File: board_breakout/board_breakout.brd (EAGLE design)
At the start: 160 x 100 mm, 3 parts

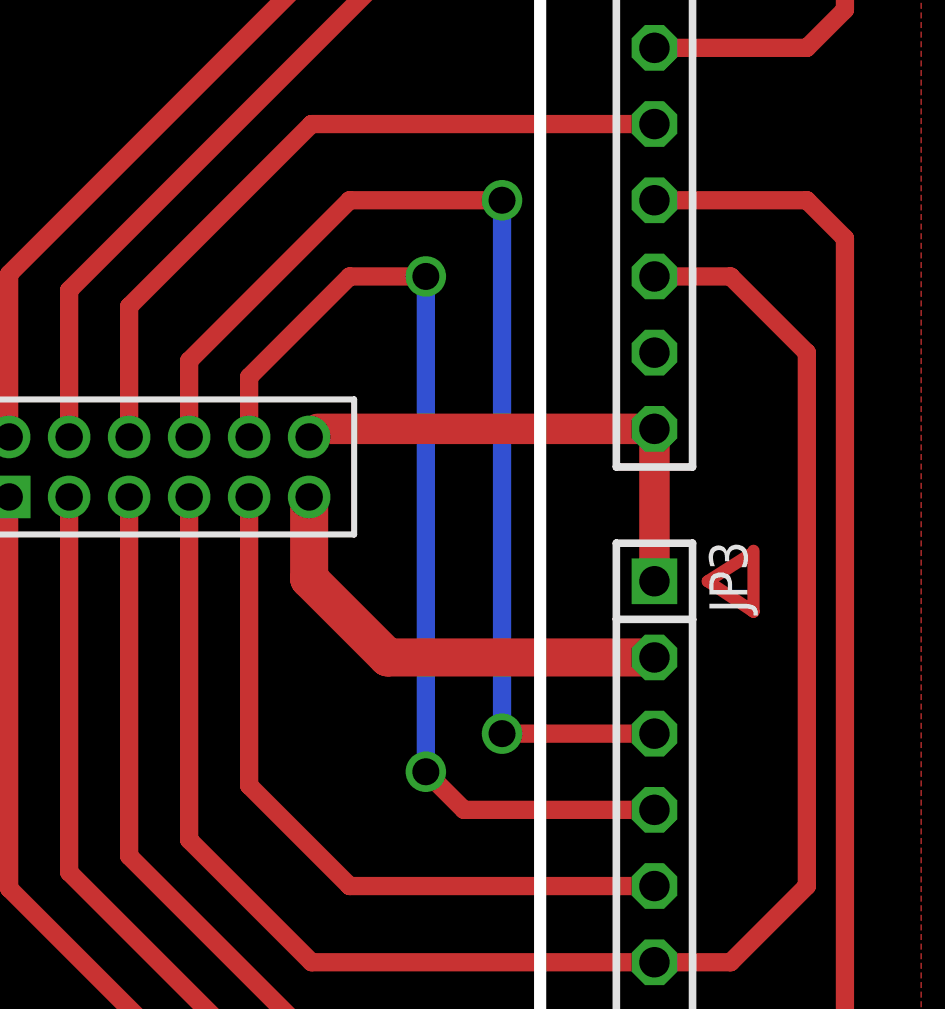
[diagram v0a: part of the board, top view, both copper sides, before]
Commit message: breakout board now one-sided
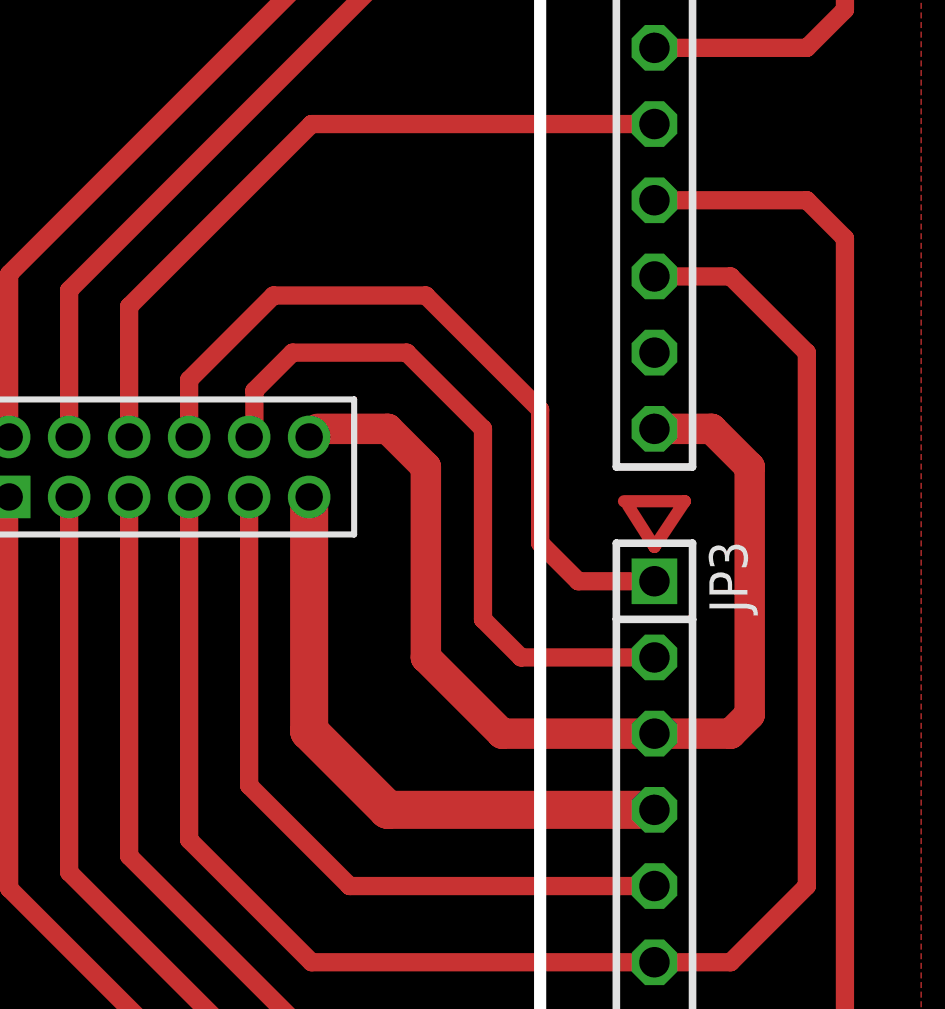
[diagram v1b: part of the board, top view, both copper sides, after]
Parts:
- JP2: value JTAG -> JTAG_Bottom
- JP3: value (none) -> Periph_Bottom
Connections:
- net 3V3: now also JP3.4; no longer JP3.2
- net GND: now also JP3.3; no longer JP3.1
- net SCL-EXT: now also JP3.2; no longer JP3.4
- net TX: now also JP3.1; no longer JP3.3
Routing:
- net GND: track 16.7 -> 34.9 mm
- net TX: track 38.0 -> 25.1 mm, vias 2 -> 0
- net SCL-EXT: track 33.9 -> 23.4 mm, vias 2 -> 0
- net 3V3: track 15.3 -> 20.4 mm
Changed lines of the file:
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@@
 <setting verticaltext="up"/>
 </settings>
-<grid distance="50" unitdist="mil" unit="mil" style="lines" multiple="1" display="no" altdistance="0.025" altunitdist="inch" altunit="inch"/>
+<grid distance="25" unitdist="mil" unit="mil" style="lines" multiple="1" display="no" altdistance="0.025" altunitdist="inch" altunit="inch"/>
 <layers>
 <layer number="1" name="Top" color="4" fill="1" visible="yes" active="yes"/>
@@
 </class>
 </classes>
-<designrules name="default">
+<designrules name="default *">
 <description language="de">&lt;b&gt;EAGLE Design Rules&lt;/b&gt;
 &lt;p&gt;
@@
 <param name="mtCopper" value="0.035mm 0.035mm 0.035mm 0.035mm 0.035mm 0.035mm 0.035mm 0.035mm 0.035mm 0.035mm 0.035mm 0.035mm 0.035mm 0.035mm 0.035mm 0.035mm"/>
 <param name="mtIsolate" value="1.5mm 0.15mm 0.2mm 0.15mm 0.2mm 0.15mm 0.2mm 0.15mm 0.2mm 0.15mm 0.2mm 0.15mm 0.2mm 0.15mm 0.2mm"/>
-<param name="mdWireWire" value="8mil"/>
-<param name="mdWirePad" value="8mil"/>
-<param name="mdWireVia" value="8mil"/>
-<param name="mdPadPad" value="8mil"/>
-<param name="mdPadVia" value="8mil"/>
-<param name="mdViaVia" value="8mil"/>
-<param name="mdSmdPad" value="8mil"/>
-<param name="mdSmdVia" value="8mil"/>
-<param name="mdSmdSmd" value="8mil"/>
+<param name="mdWireWire" value="12mil"/>
+<param name="mdWirePad" value="12mil"/>
+<param name="mdWireVia" value="12mil"/>
+<param name="mdPadPad" value="12mil"/>
+<param name="mdPadVia" value="12mil"/>
+<param name="mdViaVia" value="12mil"/>
+<param name="mdSmdPad" value="12mil"/>
+<param name="mdSmdVia" value="12mil"/>
+<param name="mdSmdSmd" value="12mil"/>
 <param name="mdViaViaSameLayer" value="8mil"/>
 <param name="mnLayersViaInSmd" value="2"/>
 <param name="mdCopperDimension" value="40mil"/>
-<param name="mdDrill" value="8mil"/>
+<param name="mdDrill" value="12mil"/>
 <param name="mdSmdStop" value="0mil"/>
 <param name="msWidth" value="10mil"/>
@@
 <elements>
 <element name="JP1" library="pinhead" package="2X06M" value="SKYNET" x="40.64" y="46.99"/>
-<element name="JP2" library="pinhead" package="1X08" value="JTAG" x="57.15" y="57.15" rot="R270"/>
-<element name="JP3" library="pinhead" package="1X10" value="" x="57.15" y="31.75" rot="R270"/>
+<element name="JP2" library="pinhead" package="1X08" value="JTAG_Bottom" x="57.15" y="57.15" rot="R270"/>
+<element name="JP3" library="pinhead" package="1X10" value="Periph_Bottom" x="57.15" y="31.75" rot="R270"/>
 </elements>
 <signals>
 <signal name="3V3">
 <contactref element="JP1" pad="11"/>
-<contactref element="JP3" pad="2"/>
-<wire x1="45.64" y1="45.99" x2="45.64" y2="43.26" width="1.27" layer="1"/>
-<wire x1="45.64" y1="43.26" x2="48.26" y2="40.64" width="1.27" layer="1"/>
-<wire x1="48.26" y1="40.64" x2="57.15" y2="40.64" width="1.27" layer="1"/>
+<contactref element="JP3" pad="4"/>
+<wire x1="45.64" y1="45.99" x2="45.64" y2="38.18" width="1.27" layer="1"/>
+<wire x1="45.64" y1="38.18" x2="48.26" y2="35.56" width="1.27" layer="1"/>
+<wire x1="48.26" y1="35.56" x2="57.15" y2="35.56" width="1.27" layer="1"/>
 </signal>
 <signal name="GND">
 <contactref element="JP1" pad="12"/>
 <contactref element="JP2" pad="8"/>
-<wire x1="57.15" y1="48.26" x2="45.91" y2="48.26" width="1.016" layer="1"/>
 <wire x1="45.91" y1="48.26" x2="45.64" y2="47.99" width="0.6096" layer="1"/>
-<contactref element="JP3" pad="1"/>
-<wire x1="57.15" y1="48.26" x2="57.15" y2="43.18" width="1.016" layer="1"/>
 <polygon width="0.4064" layer="1" isolate="1.016" orphans="yes">
 <vertex x="33.02" y="71.12"/>
@@
 <vertex x="33.02" y="72.39"/>
 </polygon>
+<contactref element="JP3" pad="3"/>
+<wire x1="45.91" y1="48.26" x2="48.26" y2="48.26" width="1.016" layer="1"/>
+<wire x1="48.26" y1="48.26" x2="49.53" y2="46.99" width="1.016" layer="1"/>
+<wire x1="49.53" y1="46.99" x2="49.53" y2="40.64" width="1.016" layer="1"/>
+<wire x1="49.53" y1="40.64" x2="52.07" y2="38.1" width="1.016" layer="1"/>
+<wire x1="52.07" y1="38.1" x2="57.15" y2="38.1" width="1.016" layer="1"/>
+<wire x1="57.15" y1="48.26" x2="59.055" y2="48.26" width="1.016" layer="1"/>
+<wire x1="59.055" y1="48.26" x2="60.325" y2="46.99" width="1.016" layer="1"/>
+<wire x1="60.325" y1="46.99" x2="60.325" y2="38.735" width="1.016" layer="1"/>
+<wire x1="60.325" y1="38.735" x2="59.69" y2="38.1" width="1.016" layer="1"/>
+<wire x1="59.69" y1="38.1" x2="57.15" y2="38.1" width="1.016" layer="1"/>
 </signal>
 <signal name="TX">
 <contactref element="JP1" pad="8"/>
-<wire x1="41.64" y1="47.99" x2="41.64" y2="50.53" width="0.6096" layer="1"/>
-<wire x1="41.64" y1="50.53" x2="46.99" y2="55.88" width="0.6096" layer="1"/>
-<wire x1="46.99" y1="55.88" x2="52.07" y2="55.88" width="0.6096" layer="1"/>
-<via x="52.07" y="55.88" extent="1-16" drill="0.9"/>
-<contactref element="JP3" pad="3"/>
-<wire x1="57.15" y1="38.1" x2="52.07" y2="38.1" width="0.6096" layer="1"/>
-<via x="52.07" y="38.1" extent="1-16" drill="0.9"/>
-<wire x1="52.07" y1="38.1" x2="52.07" y2="55.88" width="0.6096" layer="16"/>
+<contactref element="JP3" pad="1"/>
+<wire x1="41.64" y1="47.99" x2="41.64" y2="49.895" width="0.6096" layer="1"/>
+<wire x1="41.64" y1="49.895" x2="44.45" y2="52.705" width="0.6096" layer="1"/>
+<wire x1="44.45" y1="52.705" x2="49.53" y2="52.705" width="0.6096" layer="1"/>
+<wire x1="49.53" y1="52.705" x2="53.34" y2="48.895" width="0.6096" layer="1"/>
+<wire x1="53.34" y1="48.895" x2="53.34" y2="44.45" width="0.6096" layer="1"/>
+<wire x1="53.34" y1="44.45" x2="54.61" y2="43.18" width="0.6096" layer="1"/>
+<wire x1="54.61" y1="43.18" x2="57.15" y2="43.18" width="0.6096" layer="1"/>
 </signal>
 <signal name="JTAG_TDO">
@@
 <signal name="SCL-EXT">
 <contactref element="JP1" pad="10"/>
-<wire x1="43.64" y1="47.99" x2="43.64" y2="49.99" width="0.6096" layer="1"/>
-<wire x1="43.64" y1="49.99" x2="46.99" y2="53.34" width="0.6096" layer="1"/>
-<wire x1="46.99" y1="53.34" x2="49.53" y2="53.34" width="0.6096" layer="1"/>
-<via x="49.53" y="53.34" extent="1-16" drill="0.9"/>
-<contactref element="JP3" pad="4"/>
-<wire x1="57.15" y1="35.56" x2="50.8" y2="35.56" width="0.6096" layer="1"/>
-<wire x1="50.8" y1="35.56" x2="49.53" y2="36.83" width="0.6096" layer="1"/>
-<via x="49.53" y="36.83" extent="1-16" drill="0.9"/>
-<wire x1="49.53" y1="36.83" x2="49.53" y2="53.34" width="0.6096" layer="16"/>
+<contactref element="JP3" pad="2"/>
+<wire x1="57.15" y1="40.64" x2="52.705" y2="40.64" width="0.6096" layer="1"/>
+<wire x1="52.705" y1="40.64" x2="51.435" y2="41.91" width="0.6096" layer="1"/>
+<wire x1="51.435" y1="41.91" x2="51.435" y2="48.26" width="0.6096" layer="1"/>
+<wire x1="51.435" y1="48.26" x2="48.895" y2="50.8" width="0.6096" layer="1"/>
+<wire x1="48.895" y1="50.8" x2="45.085" y2="50.8" width="0.6096" layer="1"/>
+<wire x1="45.085" y1="50.8" x2="43.815" y2="49.53" width="0.6096" layer="1"/>
+<wire x1="43.815" y1="49.53" x2="43.815" y2="48.165" width="0.6096" layer="1"/>
+<wire x1="43.815" y1="48.165" x2="43.64" y2="47.99" width="0.6096" layer="1"/>
 </signal>
 <signal name="N$8">
@@
 </signal>
 <signal name="N$2">
-<wire x1="60.452" y1="44.196" x2="60.452" y2="42.164" width="0.4064" layer="1"/>
-<wire x1="60.452" y1="42.164" x2="58.928" y2="43.18" width="0.4064" layer="1"/>
-<wire x1="58.928" y1="43.18" x2="60.325" y2="44.069" width="0.4064" layer="1"/>
+<wire x1="56.134" y1="45.847" x2="58.166" y2="45.847" width="0.4064" layer="1"/>
+<wire x1="58.166" y1="45.847" x2="57.15" y2="44.323" width="0.4064" layer="1"/>
+<wire x1="57.15" y1="44.323" x2="56.261" y2="45.72" width="0.4064" layer="1"/>
 </signal>
 </signals>

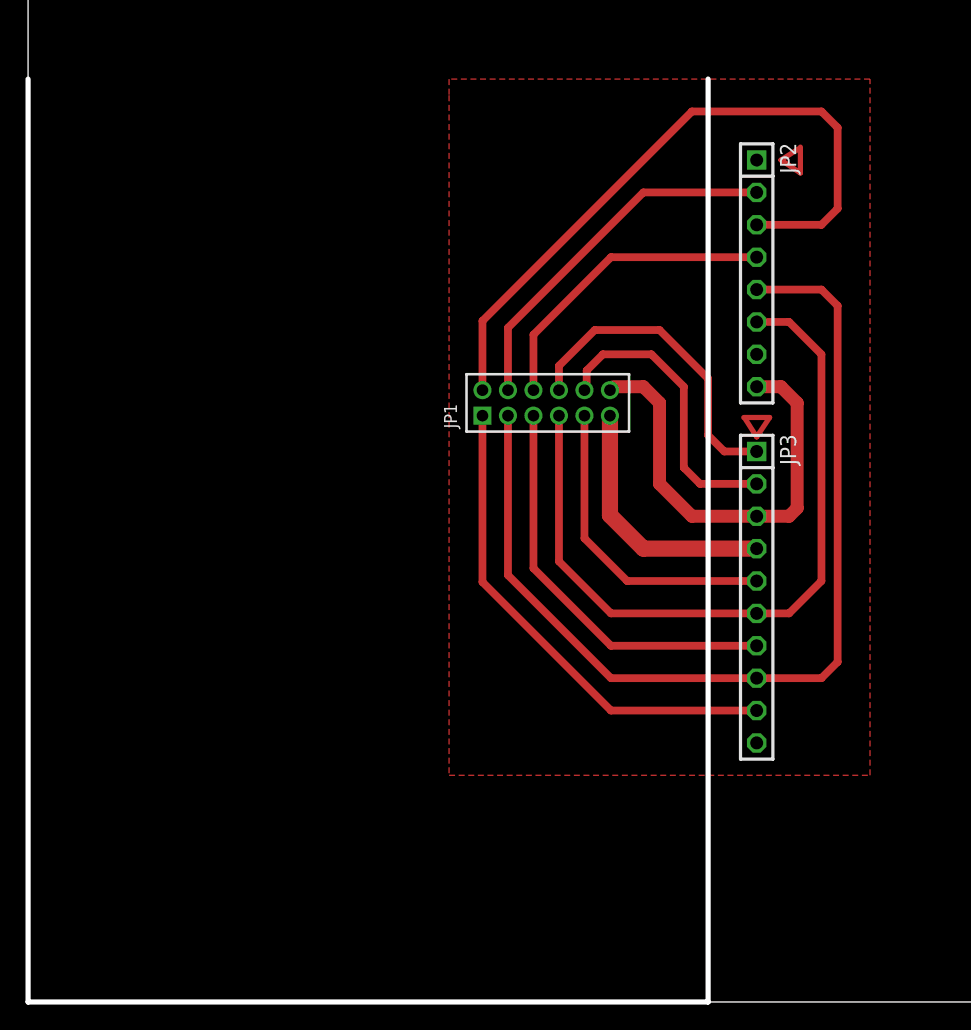
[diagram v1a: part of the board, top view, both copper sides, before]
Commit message: breakout board added header
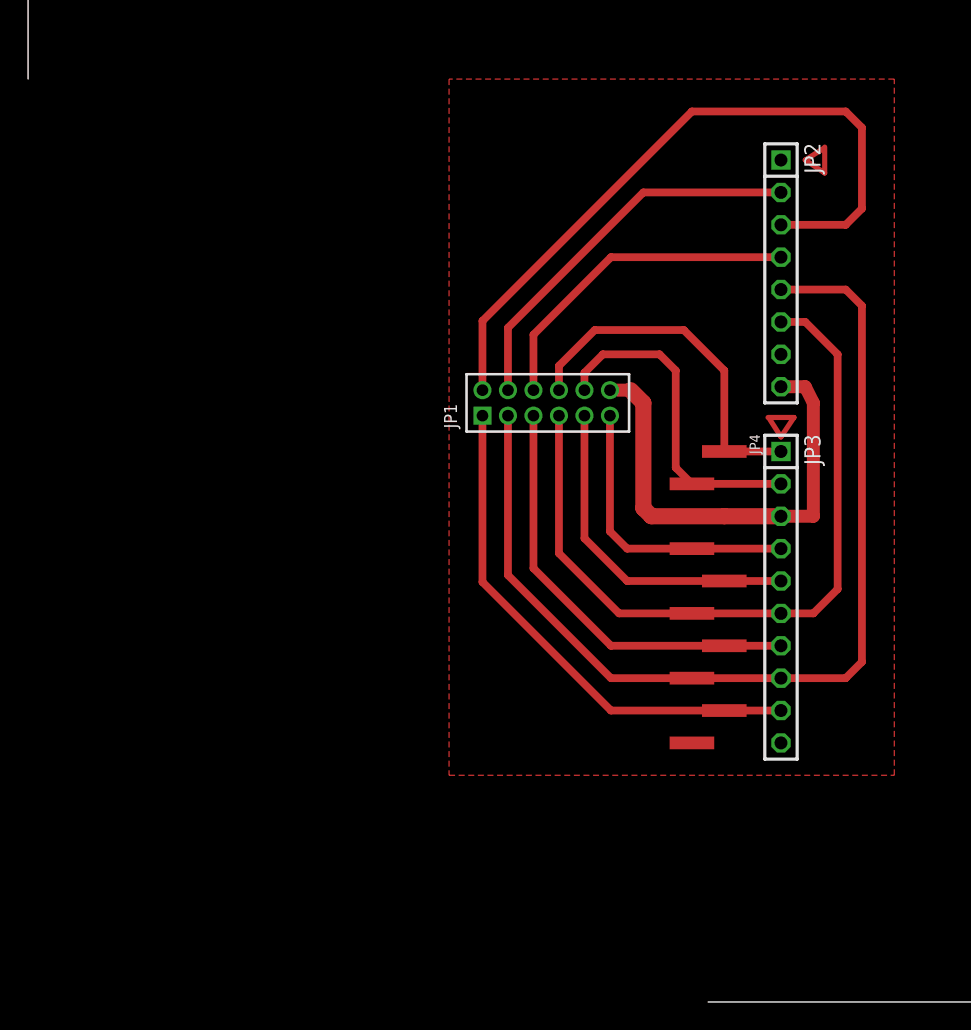
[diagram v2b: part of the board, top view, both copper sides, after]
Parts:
- added JP4: Periph_Top, microbuilder:1X10_SMT
- moved JP2 1.91 mm to (59.1, 57.1)
- moved JP3 1.91 mm to (59.1, 31.8)
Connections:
- removed net N$10: JP3.8
- removed net N$8: JP3.6
- net 3V3: now also JP4.4
- net AD-EXT: now also JP4.9
- net GND: now also JP4.3
- net JTAG_TDI: now also JP3.8, JP4.8
- net RESET: now also JP3.6, JP4.6
- net RX: now also JP4.7
- net SCL-EXT: now also JP4.2
- net SDA-EXT: now also JP4.5
- net TX: now also JP4.1
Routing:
- net TX: track 25.1 -> 28.1 mm
- net 3V3: track 20.4 -> 23.1 mm
- net SCL-EXT: track 23.4 -> 26.1 mm
- net GND: track 34.9 -> 37.1 mm
- net SDA-EXT: track 24.5 -> 26.4 mm
- net RX: track 32.0 -> 33.9 mm
- net JTAG_TMS: track 28.8 -> 30.7 mm
- net JTAG_TDO: track 24.4 -> 26.3 mm
- net AD-EXT: track 38.7 -> 40.6 mm
- net JTAG_TCK: track 53.8 -> 55.8 mm
- net JTAG_TDI: track 77.1 -> 79.0 mm
- net RESET: track 58.7 -> 59.3 mm
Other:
- outline, holes or cut-outs redrawn
